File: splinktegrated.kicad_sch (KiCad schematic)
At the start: 51 parts, among them J1 USB_C_Receptacle_USB2.0, J10 Ribbon, J11 Serial, J12 Conn_01x04_Female, J13 Conn_01x02_Female, J2 Conn_01x04_Female, J3 Conn_01x04_Female, J4 Conn_01x04_Female, J5 Conn_01x02, J6 Serial, J7 trackball, J8 Ribbon, J9 RGB, SW1 SW_SPST, SW2 SW_SPST, U1 RP2040, U2 GD25Q80CEIGR, U3 XC6210B332MR-G, U4 USBLC6-2P6, Y1 Crystal_GND24

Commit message: exclude components from BOM
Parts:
- J10, J11, J12, J13, J2, J3, J4, J6, J7, J8, J9, JP1, JP2, SW1, SW2: now left out of the parts list
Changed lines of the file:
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@@
   )
   (symbol (lib_id "Connector:Conn_01x05_Female") (at 407.67 31.75 0) (unit 1)
-    (in_bom yes) (on_board yes) (dnp no)
+    (in_bom no) (on_board yes) (dnp no)
     (property "Reference" "J10" (at 406.4 22.86 0)
       (effects (font (size 1.27 1.27)) (justify left))
@@
   )
   (symbol (lib_id "Switch:SW_SPST") (at 48.895 214.63 0) (unit 1)
-    (in_bom yes) (on_board yes) (dnp no)
+    (in_bom no) (on_board yes) (dnp no)
     (property "Reference" "SW1" (at 48.895 208.28 0)
       (effects (font (size 1.27 1.27)))
@@
   )
   (symbol (lib_id "Jumper:Jumper_2_Open") (at 330.2 91.44 0) (unit 1)
-    (in_bom yes) (on_board yes) (dnp no) (fields_autoplaced)
+    (in_bom no) (on_board yes) (dnp no) (fields_autoplaced)
     (property "Reference" "JP1" (at 330.2 85.09 0)
       (effects (font (size 1.27 1.27)))
@@
   )
   (symbol (lib_id "Connector:Conn_01x04_Female") (at -62.23 69.215 0) (unit 1)
-    (in_bom yes) (on_board yes) (dnp no) (fields_autoplaced)
+    (in_bom no) (on_board yes) (dnp no) (fields_autoplaced)
     (property "Reference" "J2" (at -60.96 69.2149 0)
       (effects (font (size 1.27 1.27)) (justify left))
@@
   )
   (symbol (lib_id "Jumper:Jumper_2_Open") (at 378.46 92.71 0) (unit 1)
-    (in_bom yes) (on_board yes) (dnp no) (fields_autoplaced)
+    (in_bom no) (on_board yes) (dnp no) (fields_autoplaced)
     (property "Reference" "JP2" (at 378.46 86.36 0)
       (effects (font (size 1.27 1.27)))
@@
   )
   (symbol (lib_id "Switch:SW_SPST") (at 49.53 205.105 0) (unit 1)
-    (in_bom yes) (on_board yes) (dnp no)
+    (in_bom no) (on_board yes) (dnp no)
     (property "Reference" "SW2" (at 49.53 198.755 0)
       (effects (font (size 1.27 1.27)))
@@
   )
   (symbol (lib_id "Connector:Conn_01x03_Female") (at 388.62 33.02 0) (unit 1)
-    (in_bom yes) (on_board yes) (dnp no)
+    (in_bom no) (on_board yes) (dnp no)
     (property "Reference" "J9" (at 389.3313 32.3278 0)
       (effects (font (size 1.27 1.27)) (justify left))
@@
   )
   (symbol (lib_id "Connector:Conn_01x04_Female") (at 41.91 40.005 0) (unit 1)
-    (in_bom yes) (on_board yes) (dnp no) (fields_autoplaced)
+    (in_bom no) (on_board yes) (dnp no) (fields_autoplaced)
     (property "Reference" "J4" (at 43.18 40.0049 0)
       (effects (font (size 1.27 1.27)) (justify left))
@@
   )
   (symbol (lib_id "Connector:Conn_01x06_Female") (at 368.3 60.96 0) (unit 1)
-    (in_bom yes) (on_board yes) (dnp no)
+    (in_bom no) (on_board yes) (dnp no)
     (property "Reference" "J8" (at 367.03 52.07 0)
       (effects (font (size 1.27 1.27)) (justify left))
@@
   )
   (symbol (lib_id "Connector:Conn_01x04_Female") (at -61.595 82.55 0) (unit 1)
-    (in_bom yes) (on_board yes) (dnp no) (fields_autoplaced)
+    (in_bom no) (on_board yes) (dnp no) (fields_autoplaced)
     (property "Reference" "J3" (at -60.325 82.5499 0)
       (effects (font (size 1.27 1.27)) (justify left))
@@
   )
   (symbol (lib_id "Connector:AudioJack4") (at 368.3 87.63 0) (unit 1)
-    (in_bom yes) (on_board yes) (dnp no)
+    (in_bom no) (on_board yes) (dnp no)
     (property "Reference" "J11" (at 367.157 79.5082 0)
       (effects (font (size 1.27 1.27)))
@@
   )
   (symbol (lib_id "Connector:Conn_01x06_Female") (at 367.03 31.75 0) (unit 1)
-    (in_bom yes) (on_board yes) (dnp no)
+    (in_bom no) (on_board yes) (dnp no)
     (property "Reference" "J7" (at 368.3 33.02 0)
       (effects (font (size 1.27 1.27)) (justify left))
@@
   )
   (symbol (lib_id "Connector:Conn_01x02_Female") (at 45.085 175.895 0) (unit 1)
-    (in_bom yes) (on_board yes) (dnp no)
+    (in_bom no) (on_board yes) (dnp no)
     (property "Reference" "J13" (at 46.99 175.8949 0)
       (effects (font (size 1.27 1.27)) (justify left))
@@
   )
   (symbol (lib_id "Connector:AudioJack4") (at 320.04 86.36 0) (unit 1)
-    (in_bom yes) (on_board yes) (dnp no)
+    (in_bom no) (on_board yes) (dnp no)
     (property "Reference" "J6" (at 318.897 78.2382 0)
       (effects (font (size 1.27 1.27)))
@@
   )
   (symbol (lib_id "Connector:Conn_01x04_Female") (at 42.545 53.34 0) (unit 1)
-    (in_bom yes) (on_board yes) (dnp no) (fields_autoplaced)
+    (in_bom no) (on_board yes) (dnp no) (fields_autoplaced)
     (property "Reference" "J12" (at 43.815 53.3399 0)
       (effects (font (size 1.27 1.27)) (justify left))

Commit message: memory, data line protection
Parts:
- removed U2: GD25Q80CEIGR, 0xLib_Package_DFN_QFN:USON-8-1EP_3x2mm_P0.5mm_EP0.25x1.65mm, symbol Memory_Flash:W25Q32JVZP
- added R12: 120, Resistor_SMD:R_0402_1005Metric, symbol Device:R
- added U2: USBLC6-2P6, Package_TO_SOT_SMD:SOT-666, symbol Power_Protection:USBLC6-2P6
- added U5: W25Q128JVS, drawings:W25Q128JVPIQ, symbol Memory_Flash:W25Q128JVS
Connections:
- net +3V3: now also U2.5 (VBUS), U5.8 (VCC)
- net GND: now also U2.2 (GND), U5.4 (GND)
- net QSPI_D0: now also U5.5 (DI(IO0))
- net QSPI_D1: now also U5.2 (DO(IO1))
- net QSPI_D2: now also U5.3 (IO2)
- net QSPI_D3: now also U5.7 (IO3)
- net QSPI_SCLK: now also U5.6 (CLK)
- net QSPI_~{CS}: now also U5.1 (~{CS})
- net serial_l: now also R12.2; no longer J11.R2, J6.R2
- new net: J11.R2, J6.R2, R12.1, U2.1 (I/O1), U2.6 (I/O1)
- no-connect marks 16 -> 18
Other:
- note added: "Serial and protection"
- moved on the sheet: J10, J11, J6, J7, J8, J9, JP1, JP2

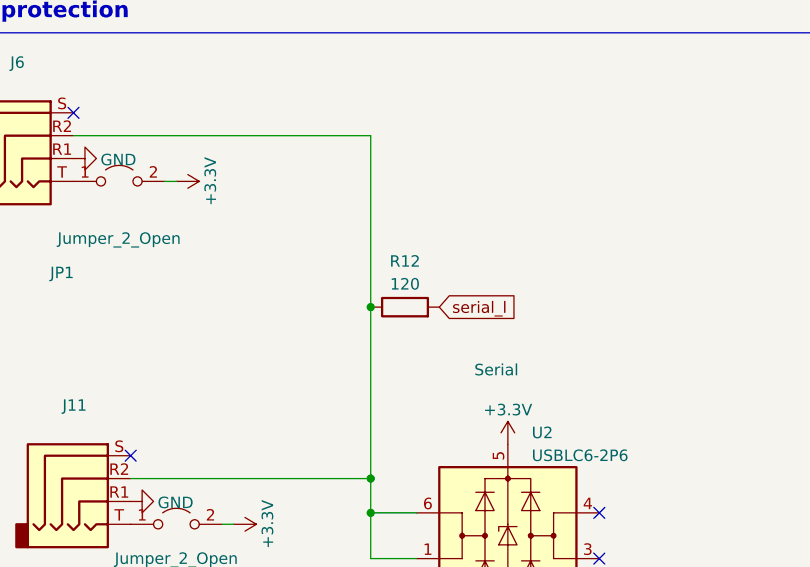
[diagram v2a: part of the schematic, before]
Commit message: remove serial resistor
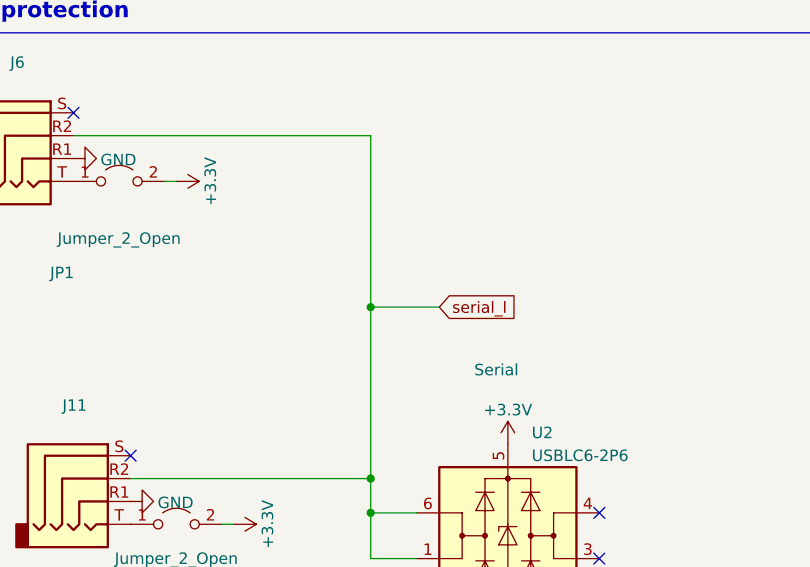
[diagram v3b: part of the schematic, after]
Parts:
- removed R12: 120, Resistor_SMD:R_0402_1005Metric, symbol Device:R
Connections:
- net serial_l: now also J11.R2, J6.R2, U2.1 (I/O1), U2.6 (I/O1)
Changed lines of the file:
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@@
     (company "bastardkb")
   )
-  (junction (at 354.33 113.03) (diameter 0) (color 0 0 0 0)
-  )
   (junction (at 46.99 127) (diameter 0) (color 0 0 0 0)
   )
@@
   (junction (at 111.76 96.52) (diameter 0) (color 0 0 0 0)
   )
+  (junction (at 354.33 113.03) (diameter 0) (color 0 0 0 0)
+  )
   (junction (at 157.48 185.42) (diameter 0) (color 0 0 0 0)
   )
@@
     (stroke (width 0) (type default))
   )
-  (wire (pts (xy 354.33 113.03) (xy 354.33 132.08))
+  (wire (pts (xy 354.33 93.98) (xy 354.33 113.03))
     (stroke (width 0) (type default))
   )
@@
     (stroke (width 0) (type default))
   )
-  (wire (pts (xy 354.33 93.98) (xy 354.33 113.03))
-    (stroke (width 0) (type default))
-  )
   (wire (pts (xy 97.79 97.79) (xy 97.79 96.52))
     (stroke (width 0) (type default))
@@
     (stroke (width 0) (type default))
   )
+  (wire (pts (xy 354.33 113.03) (xy 361.95 113.03))
+    (stroke (width 0) (type default))
+  )
   (wire (pts (xy 182.88 78.74) (xy 191.77 78.74))
     (stroke (width 0) (type default))
@@
     (stroke (width 0) (type default))
   )
+  (wire (pts (xy 354.33 113.03) (xy 354.33 132.08))
+    (stroke (width 0) (type default))
+  )
   (wire (pts (xy 160.02 38.1) (xy 162.56 38.1))
     (stroke (width 0) (type default))
@@
         )
       )
-    )
-  )
-  (symbol (lib_id "Device:R") (at 358.14 113.03 90) (unit 1)
-    (in_bom yes) (on_board yes) (dnp no) (fields_autoplaced)
-    (property "Reference" "R12" (at 358.14 107.95 90)
-      (effects (font (size 1.27 1.27)))
-    )
-    (property "Value" "120" (at 358.14 110.49 90)
-      (effects (font (size 1.27 1.27)))
-    )
-    (property "Footprint" "Resistor_SMD:R_0402_1005Metric" (at 358.14 114.808 90)
-      (effects (font (size 1.27 1.27)) hide)
-    )
-    (property "Datasheet" "~" (at 358.14 113.03 0)
-      (effects (font (size 1.27 1.27)) hide)
-    )
-    (pin "1")
-    (pin "2")
-    (instances
-      (project "splinktegrated"
-        (path "/7353e96a-343a-4876-b497-b1d205a14d97"
-          (reference "R12") (unit 1)
-        )
-      )

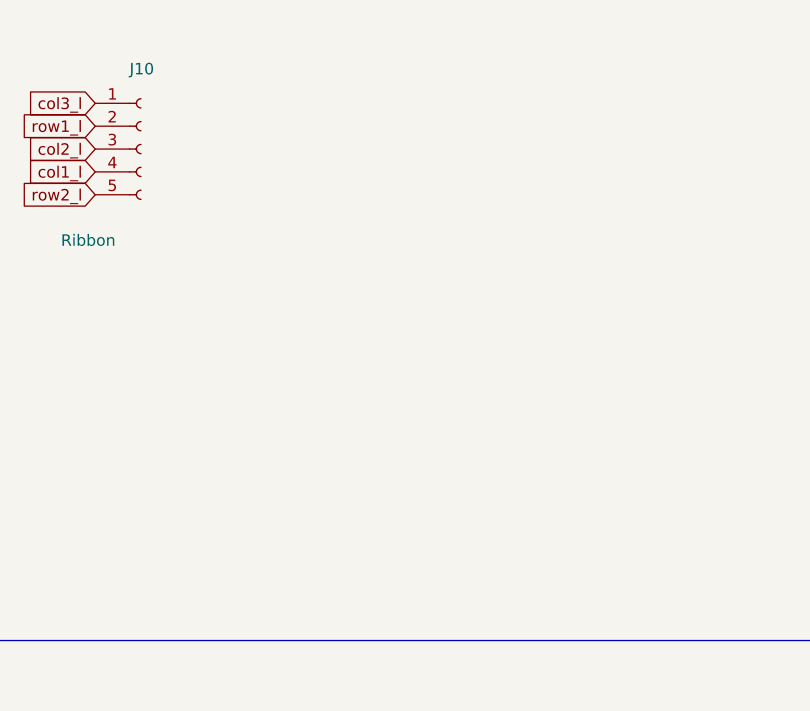
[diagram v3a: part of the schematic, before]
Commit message: add fpc connector
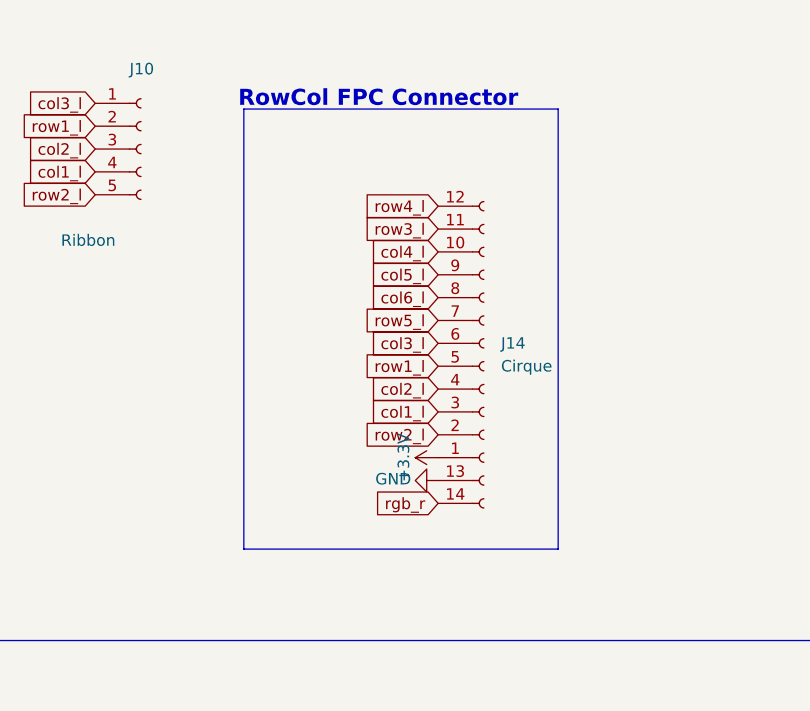
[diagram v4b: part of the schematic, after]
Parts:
- added J14: Cirque, local-libraries:FPC-SMD_FPC05012-09200-.5mm, symbol Connector:Conn_01x14_Female
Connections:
- net +3V3: now also J14.1 (Pin_1)
- net GND: now also J14.13 (Pin_13)
- net col1_l: now also J14.3 (Pin_3)
- net col2_l: now also J14.4 (Pin_4)
- net col3_l: now also J14.6 (Pin_6)
- net col4_l: now also J14.10 (Pin_10)
- net col5_l: now also J14.9 (Pin_9)
- net col6_l: now also J14.8 (Pin_8)
- net rgb_r: now also J14.14 (Pin_14)
- net row1_l: now also J14.5 (Pin_5)
- net row2_l: now also J14.2 (Pin_2)
- net row3_l: now also J14.11 (Pin_11)
- net row4_l: now also J14.12 (Pin_12)
- net row5_l: now also J14.7 (Pin_7)
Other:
- note added: "RowCol FPC Connector"
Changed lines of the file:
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@@
+    (stroke (width 0) (type default))
+  )
+  (polyline (pts (xy 369.57 23.495) (xy 369.57 72.39))
     (stroke (width 0) (type default))
   )
@@
     (stroke (width 0) (type default))
   )
+  (polyline (pts (xy 369.57 23.495) (xy 404.495 23.495))
+    (stroke (width 0) (type default))
+  )
   (polyline (pts (xy 279.4 96.52) (xy 279.4 20.32))
     (stroke (width 0) (type default))
@@
     (stroke (width 0) (type default))
   )
+  (polyline (pts (xy 404.495 23.495) (xy 404.495 72.39))
+    (stroke (width 0) (type default))
+  )
   (wire (pts (xy 198.12 97.155) (xy 198.12 98.425))
     (stroke (width 0) (type default))
@@
   )
   (wire (pts (xy 152.4 38.1) (xy 154.94 38.1))
+    (stroke (width 0) (type default))
+  )
+  (polyline (pts (xy 404.495 72.39) (xy 369.57 72.39))
     (stroke (width 0) (type default))
   )
@@
     (effects (font (size 1.778 1.778) (thickness 0.3556) bold) (justify left bottom))
   )
+  (text "RowCol FPC Connector" (at 368.935 23.495 0)
+    (effects (font (size 1.778 1.778) (thickness 0.3556) bold) (justify left bottom))
+  )
   (text "Headers" (at -81.28 62.865 0)
     (effects (font (size 1.778 1.778) (thickness 0.3556) bold) (justify left bottom))
@@
   (label "A1" (at 255.27 54.61 0) (fields_autoplaced)
     (effects (font (size 1.27 1.27)) (justify left bottom))
+  )
+  (global_label "row5_l" (shape input) (at 391.16 46.99 180)
+    (effects (font (size 1.27 1.27)) (justify right))
+    (property "Intersheetrefs" "${INTERSHEET_REFS}" (at 361.95 -20.32 0)
+      (effects (font (size 1.27 1.27)) hide)
+    )
   )
   (global_label "row3_l" (shape input) (at 313.69 54.61 180)
@@
     )
   )
+  (global_label "col1_l" (shape input) (at 391.16 57.15 180)
+    (effects (font (size 1.27 1.27)) (justify right))
+    (property "Intersheetrefs" "${INTERSHEET_REFS}" (at 361.95 10.16 0)
+      (effects (font (size 1.27 1.27)) hide)
+    )
+  )
   (global_label "col4_l" (shape input) (at 228.6 59.69 180)
     (effects (font (size 1.27 1.27)) (justify right))
@@
     (effects (font (size 1.27 1.27)) (justify right))
     (property "Intersheetrefs" "${INTERSHEET_REFS}" (at 284.48 -2.54 0)
+      (effects (font (size 1.27 1.27)) hide)
+    )
+  )
+  (global_label "row1_l" (shape input) (at 391.16 52.07 180)
+    (effects (font (size 1.27 1.27)) (justify right))
+    (property "Intersheetrefs" "${INTERSHEET_REFS}" (at 361.95 10.16 0)
+      (effects (font (size 1.27 1.27)) hide)
+    )
+  )
+  (global_label "col3_l" (shape input) (at 391.16 49.53 180)
+    (effects (font (size 1.27 1.27)) (justify right))
+    (property "Intersheetrefs" "${INTERSHEET_REFS}" (at 361.95 10.16 0)
       (effects (font (size 1.27 1.27)) hide)
     )
@@
     (effects (font (size 1.27 1.27)) (justify right))
     (property "Intersheetrefs" "${INTERSHEET_REFS}" (at 323.85 -16.51 0)
+      (effects (font (size 1.27 1.27)) hide)
+    )
+  )
+  (global_label "row2_l" (shape input) (at 391.16 59.69 180)
+    (effects (font (size 1.27 1.27)) (justify right))
+    (property "Intersheetrefs" "${INTERSHEET_REFS}" (at 361.95 10.16 0)
       (effects (font (size 1.27 1.27)) hide)
     )
@@
     )
   )
+  (global_label "row4_l" (shape input) (at 391.16 34.29 180)
+    (effects (font (size 1.27 1.27)) (justify right))
+    (property "Intersheetrefs" "${INTERSHEET_REFS}" (at 361.95 -20.32 0)
+      (effects (font (size 1.27 1.27)) hide)
+    )
+  )
+  (global_label "row3_l" (shape input) (at 391.16 36.83 180)
+    (effects (font (size 1.27 1.27)) (justify right))
+    (property "Intersheetrefs" "${INTERSHEET_REFS}" (at 361.95 -20.32 0)
+      (effects (font (size 1.27 1.27)) hide)
+    )
+  )
   (global_label "col2_l" (shape input) (at 264.16 52.07 0)
     (effects (font (size 1.27 1.27)) (justify left))
@@
     (effects (font (size 1.27 1.27)) (justify right))
     (property "Intersheetrefs" "${INTERSHEET_REFS}" (at 199.39 0 0)
+      (effects (font (size 1.27 1.27)) hide)
+    )
+  )
+  (global_label "col5_l" (shape input) (at 391.16 41.91 180)
+    (effects (font (size 1.27 1.27)) (justify right))
+    (property "Intersheetrefs" "${INTERSHEET_REFS}" (at 361.95 -20.32 0)
       (effects (font (size 1.27 1.27)) hide)
     )
@@
     )
   )
+  (global_label "col2_l" (shape input) (at 391.16 54.61 180)
+    (effects (font (size 1.27 1.27)) (justify right))
+    (property "Intersheetrefs" "${INTERSHEET_REFS}" (at 361.95 10.16 0)
+      (effects (font (size 1.27 1.27)) hide)
+    )
+  )
   (global_label "mosi_l" (shape input) (at 264.16 64.77 0)
     (effects (font (size 1.27 1.27)) (justify left))
@@
     )
   )
+  (global_label "rgb_r" (shape input) (at 391.16 67.31 180)
+    (effects (font (size 1.27 1.27)) (justify right))
+    (property "Intersheetrefs" "${INTERSHEET_REFS}" (at 247.015 -9.525 0)
+      (effects (font (size 1.27 1.27)) hide)
+    )
+  )
   (global_label "row3_l" (shape input) (at 228.6 57.15 180)
     (effects (font (size 1.27 1.27)) (justify right))
@@
     )
   )
+  (global_label "col6_l" (shape input) (at 391.16 44.45 180)
+    (effects (font (size 1.27 1.27)) (justify right))
+    (property "Intersheetrefs" "${INTERSHEET_REFS}" (at 361.95 -20.32 0)
+      (effects (font (size 1.27 1.27)) hide)
+    )
+  )
   (global_label "col2_l" (shape input) (at 353.06 27.94 180)
     (effects (font (size 1.27 1.27)) (justify right))
     (property "Intersheetrefs" "${INTERSHEET_REFS}" (at 323.85 -16.51 0)
+      (effects (font (size 1.27 1.27)) hide)
+    )
+  )
+  (global_label "col4_l" (shape input) (at 391.16 39.37 180)
+    (effects (font (size 1.27 1.27)) (justify right))
+    (property "Intersheetrefs" "${INTERSHEET_REFS}" (at 361.95 -20.32 0)
       (effects (font (size 1.27 1.27)) hide)
     )
@@
     )
   )
+  (symbol (lib_id "power:+3.3V") (at 391.16 62.23 90) (unit 1)
+    (in_bom yes) (on_board yes) (dnp no)
+    (property "Reference" "#PWR032" (at 394.97 62.23 0)
+      (effects (font (size 1.27 1.27)) hide)
+    )
+    (property "Value" "+3.3V" (at 387.35 62.23 0)
+      (effects (font (size 1.27 1.27)))
+    )
+    (property "Footprint" "" (at 391.16 62.23 0)
+      (effects (font (size 1.27 1.27)) hide)
+    )
+    (property "Datasheet" "" (at 391.16 62.23 0)
+      (effects (font (size 1.27 1.27)) hide)
+    )
+    (pin "1")
+    (instances
+      (project "splinktegrated"
+        (path "/7353e96a-343a-4876-b497-b1d205a14d97"
+          (reference "#PWR032") (unit 1)
+        )
+      )
+    )
+  )
   (symbol (lib_id "Connector:Conn_01x05_Female") (at 358.14 27.94 0) (unit 1)
     (in_bom no) (on_board yes) (dnp no)
@@
         (path "/7353e96a-343a-4876-b497-b1d205a14d97"
           (reference "SW1") (unit 1)
+        )
+      )
+    )
+  )
+  (symbol (lib_id "power:GND") (at 391.16 64.77 270) (unit 1)
+    (in_bom yes) (on_board yes) (dnp no)
+    (property "Reference" "#PWR034" (at 384.81 64.77 0)
+      (effects (font (size 1.27 1.27)) hide)
+    )
+    (property "Value" "GND" (at 384.1751 64.614 90)
+      (effects (font (size 1.27 1.27)) (justify left))
+    )
+    (property "Footprint" "" (at 391.16 64.77 0)
+      (effects (font (size 1.27 1.27)) hide)
+    )
+    (property "Datasheet" "" (at 391.16 64.77 0)
+      (effects (font (size 1.27 1.27)) hide)
+    )
+    (pin "1")
+    (instances
+      (project "splinktegrated"
+        (path "/7353e96a-343a-4876-b497-b1d205a14d97"
+          (reference "#PWR034") (unit 1)
         )
       )
@@
         )
       )
+    )
+  )
+  (symbol (lib_id "Connector:Conn_01x14_Female") (at 396.24 49.53 0) (unit 1)
+    (in_bom yes) (on_board yes) (dnp no) (fields_autoplaced)
+    (property "Reference" "J14" (at 398.145 49.5299 0)
+      (effects (font (size 1.27 1.27)) (justify left))
+    )
+    (property "Value" "Cirque" (at 398.145 52.0699 0)
+      (effects (font (size 1.27 1.27)) (justify left))
+    )
+    (property "Footprint" "local-libraries:FPC-SMD_FPC05012-09200-.5mm" (at 417.83 45.72 0)
+      (effects (font (size 1.27 1.27)) hide)
+    )
+    (property "Datasheet" "~" (at 396.24 49.53 0)
+      (effects (font (size 1.27 1.27)) hide)
+    )
+    (pin "1")
+    (pin "10")
+    (pin "11")
+    (pin "12")
+    (pin "13")
+    (pin "14")
+    (pin "2")
+    (pin "3")
+    (pin "4")
+    (pin "5")
+    (pin "6")
+    (pin "7")
+    (pin "8")
+    (pin "9")
+    (instances
+      (project "splinktegrated"
+        (path "/7353e96a-343a-4876-b497-b1d205a14d97"
+          (reference "J14") (unit 1)
+        )
+      )
